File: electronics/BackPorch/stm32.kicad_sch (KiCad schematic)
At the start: 32 parts, among them J1 USB_B_Micro, J10 Conn_ARM_SWD_TagConnect_TC203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, U4 USBLC6-2SC6, U5 STM32G0B1KBUx

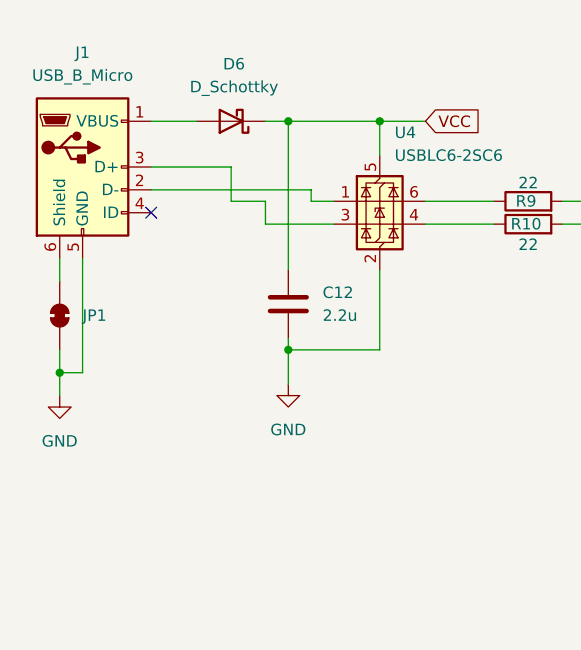
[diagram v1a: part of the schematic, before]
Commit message: Added the wpilib code. I have only tested the Java code and it works.
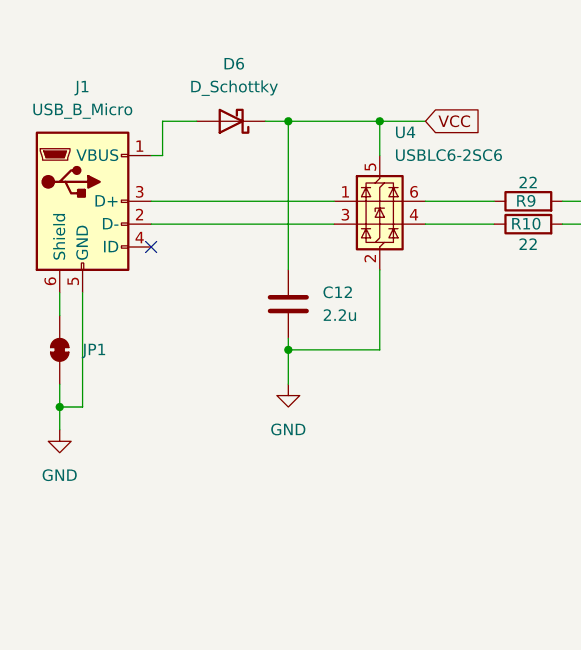
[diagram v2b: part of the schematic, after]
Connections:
- net at J1.2 (D-): now also U4.3 (I/O2); no longer U4.1 (I/O1)
- net at J1.3 (D+): now also U4.1 (I/O1); no longer U4.3 (I/O2)
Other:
- moved on the sheet: J1, JP1
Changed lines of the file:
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@@
 	)
 	(junction
-		(at 19.05 52.07)
+		(at 19.05 55.88)
 		(diameter 0)
 		(color 0 0 0 0)
@@
 	)
 	(no_connect
-		(at 29.21 34.29)
+		(at 29.21 38.1)
 	)
 	(no_connect
@@
 	(wire
 		(pts
-			(xy 29.21 24.13) (xy 34.29 24.13)
+			(xy 30.48 24.13) (xy 34.29 24.13)
 		)
 		(stroke
@@
 	(wire
 		(pts
-			(xy 128.27 85.09) (xy 134.62 85.09)
+			(xy 29.21 27.94) (xy 30.48 27.94)
 		)
 		(stroke
@@
 	(wire
 		(pts
-			(xy 147.32 44.45) (xy 147.32 48.26)
+			(xy 128.27 85.09) (xy 134.62 85.09)
 		)
 		(stroke
@@
 	(wire
 		(pts
-			(xy 46.99 33.02) (xy 46.99 31.75)
+			(xy 147.32 44.45) (xy 147.32 48.26)
 		)
 		(stroke
@@
 	(wire
 		(pts
-			(xy 128.27 95.25) (xy 134.62 95.25)
+			(xy 29.21 35.56) (xy 49.53 35.56)
 		)
 		(stroke
@@
 	(wire
 		(pts
-			(xy 41.91 35.56) (xy 41.91 33.02)
+			(xy 128.27 95.25) (xy 134.62 95.25)
 		)
 		(stroke
@@
 	(wire
 		(pts
-			(xy 19.05 39.37) (xy 19.05 41.91)
+			(xy 19.05 43.18) (xy 19.05 45.72)
 		)
 		(stroke
@@
 	(wire
 		(pts
-			(xy 49.53 33.02) (xy 46.99 33.02)
-		)
-		(stroke
-			(width 0)
-			(type default)
-		)
-	)
-	(wire
-		(pts
 			(xy 185.42 87.63) (xy 193.04 87.63)
 		)
@@
 	(wire
 		(pts
-			(xy 19.05 49.53) (xy 19.05 52.07)
+			(xy 19.05 53.34) (xy 19.05 55.88)
 		)
 		(stroke
@@
 	(wire
 		(pts
-			(xy 38.1 33.02) (xy 38.1 29.21)
-		)
-		(stroke
-			(width 0)
-			(type default)
-		)
-	)
-	(wire
-		(pts
 			(xy 74.93 35.56) (xy 83.82 35.56)
 		)
@@
 	(wire
 		(pts
-			(xy 19.05 52.07) (xy 19.05 54.61)
+			(xy 19.05 55.88) (xy 19.05 58.42)
 		)
 		(stroke
@@
 	(wire
 		(pts
-			(xy 41.91 33.02) (xy 38.1 33.02)
-		)
-		(stroke
-			(width 0)
-			(type default)
-		)
-	)
-	(wire
-		(pts
-			(xy 21.59 39.37) (xy 21.59 52.07)
+			(xy 21.59 43.18) (xy 21.59 55.88)
 		)
 		(stroke
@@
 	(wire
 		(pts
-			(xy 19.05 52.07) (xy 21.59 52.07)
+			(xy 19.05 55.88) (xy 21.59 55.88)
 		)
 		(stroke
@@
 	(wire
 		(pts
-			(xy 49.53 35.56) (xy 41.91 35.56)
+			(xy 29.21 33.02) (xy 49.53 33.02)
 		)
 		(stroke
@@
 	(wire
 		(pts
-			(xy 38.1 29.21) (xy 29.21 29.21)
-		)
-		(stroke
-			(width 0)
-			(type default)
-		)
-	)
-	(wire
-		(pts
 			(xy 128.27 102.87) (xy 134.62 102.87)
 		)
@@
 	(wire
 		(pts
-			(xy 54.61 40.64) (xy 54.61 49.53)
+			(xy 30.48 27.94) (xy 30.48 24.13)
 		)
 		(stroke
@@
 	(wire
 		(pts
-			(xy 231.14 20.32) (xy 243.84 20.32)
+			(xy 54.61 40.64) (xy 54.61 49.53)
 		)
 		(stroke
@@
 	(wire
 		(pts
-			(xy 29.21 31.75) (xy 46.99 31.75)
+			(xy 231.14 20.32) (xy 243.84 20.32)
 		)
 		(stroke
@@
 	(symbol
 		(lib_id "power:GND")
-		(at 19.05 54.61 0)
+		(at 19.05 58.42 0)
 		(unit 1)
 		(exclude_from_sim no)
@@
 		(fields_autoplaced yes)
 		(property "Reference" "#PWR013"
-			(at 19.05 60.96 0)
+			(at 19.05 64.77 0)
 			(effects
 				(font
@@
 		)
 		(property "Value" "GND"
-			(at 19.05 59.69 0)
+			(at 19.05 63.5 0)
 			(effects
 				(font
@@
 		)
 		(property "Footprint" ""
-			(at 19.05 54.61 0)
+			(at 19.05 58.42 0)
 			(effects
 				(font
@@
 		)
 		(property "Datasheet" ""
-			(at 19.05 54.61 0)
+			(at 19.05 58.42 0)
 			(effects
 				(font
@@
 		)
 		(property "Description" ""
-			(at 19.05 54.61 0)
+			(at 19.05 58.42 0)
 			(effects
 				(font
@@
 	(symbol
 		(lib_id "Connector:USB_B_Micro")
-		(at 21.59 29.21 0)
+		(at 21.59 33.02 0)
 		(unit 1)
 		(exclude_from_sim no)
@@
 		(fields_autoplaced yes)
 		(property "Reference" "J1"
-			(at 21.59 16.51 0)
+			(at 21.59 20.32 0)
 			(effects
 				(font
@@
 		)
 		(property "Value" "USB_B_Micro"
-			(at 21.59 19.05 0)
+			(at 21.59 22.86 0)
 			(effects
 				(font
@@
 		)
 		(property "Footprint" "Connector_USB:USB_Micro-B_Amphenol_10118193-0001LF_Horizontal"
-			(at 25.4 30.48 0)
+			(at 25.4 34.29 0)
 			(effects
 				(font
@@
 		)
 		(property "Datasheet" "~"
-			(at 25.4 30.48 0)
+			(at 25.4 34.29 0)
 			(effects
 				(font
@@
 		)
 		(property "Description" "USB Micro Type B connector"
-			(at 21.59 29.21 0)
+			(at 21.59 33.02 0)
 			(effects
 				(font
@@
 		)
 		(property "JLC" "C132562"
-			(at 21.59 29.21 0)
+			(at 21.59 33.02 0)
 			(effects
 				(font
@@
 	(symbol
 		(lib_id "Jumper:SolderJumper_2_Bridged")
-		(at 19.05 45.72 90)
+		(at 19.05 49.53 90)
 		(unit 1)
 		(exclude_from_sim no)
@@
 		(fields_autoplaced yes)
 		(property "Reference" "JP1"
-			(at 21.59 45.7199 90)
+			(at 21.59 49.5299 90)
 			(effects
 				(font
@@
 		)
 		(property "Value" "SolderJumper_2_Bridged"
-			(at 15.24 45.72 0)
+			(at 15.24 49.53 0)
 			(effects
 				(font
@@
 		)
 		(property "Footprint" "Jumper:SolderJumper-2_P1.3mm_Bridged2Bar_RoundedPad1.0x1.5mm"
-			(at 19.05 45.72 0)
+			(at 19.05 49.53 0)
 			(effects
 				(font
@@
 		)
 		(property "Datasheet" "~"
-			(at 19.05 45.72 0)
+			(at 19.05 49.53 0)
 			(effects
 				(font
@@
 		)
 		(property "Description" "Solder Jumper, 2-pole, closed/bridged"
-			(at 19.05 45.72 0)
+			(at 19.05 49.53 0)
 			(effects
 				(font
